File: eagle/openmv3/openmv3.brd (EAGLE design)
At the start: 35.6 x 44.5 mm, 60 parts, among them Q1 MOSFET, U1 STM32F765VGT6, U2 OV7725, U3 BD33IA, X1 47571-0001

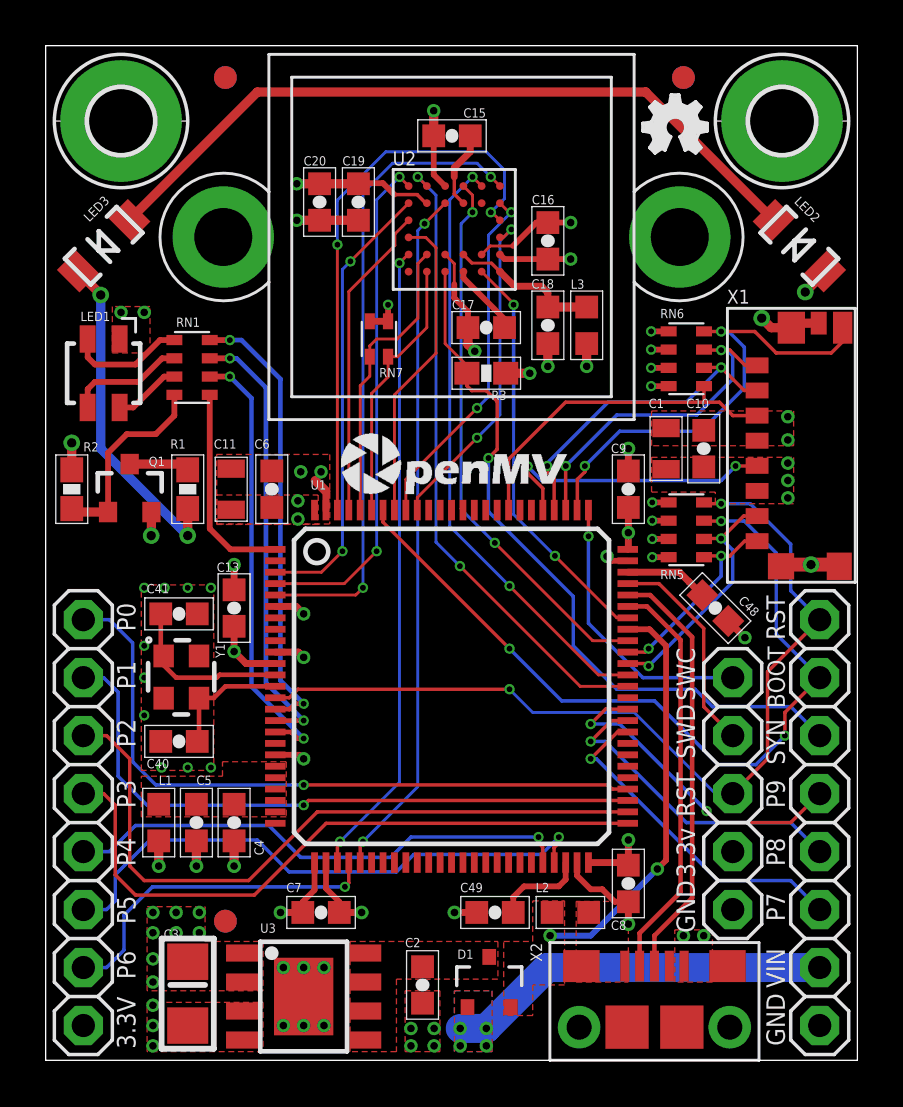
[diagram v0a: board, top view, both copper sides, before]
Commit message: Added 3 more I/O pins
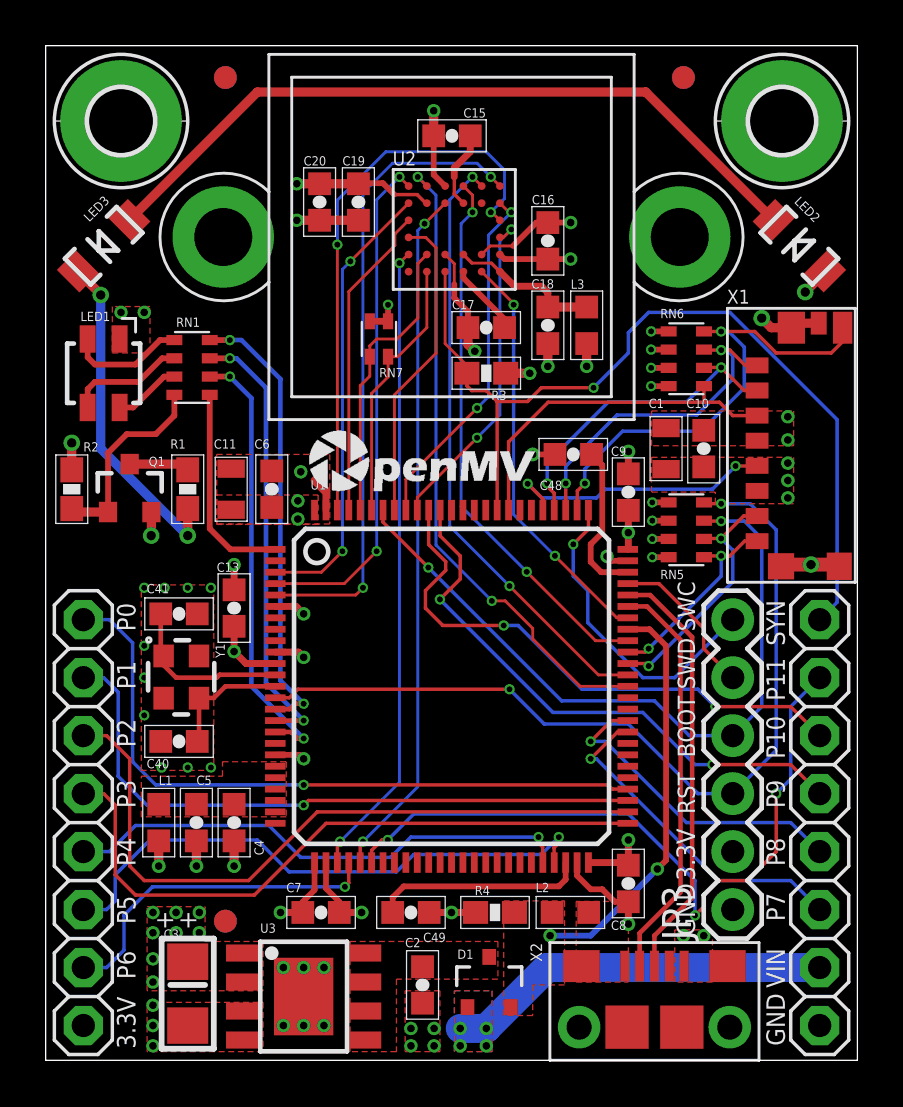
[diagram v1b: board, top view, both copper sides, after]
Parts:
- added R4: 100K, sfe:0603-RES
- JP3: device pinhead:1X05 -> SparkFun-Connectors:1X06
- moved LOGO1 38.1 mm to (20.8, 2.03), flipped to the bottom
- moved C48 9.17 mm to (23.1, 26.5), turned to 180 degrees
- moved JP3 5.08 mm to (30.1, 6.60), turned to 90 degrees
- moved C49 3.68 mm to (16.0, 6.48), turned to 0 degrees
- moved U$4 1.40 mm to (11.4, 24.8)
- moved C9 0.13 mm to (25.5, 24.9)
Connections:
- net N$1 renamed VREFH
- net N$10 renamed LED_IR_4
- net N$12 renamed VDDA
- net N$13 renamed AVDD
- net N$14 renamed LED_IR_3
- net N$15 renamed DVDD
- net N$17 renamed LED_IR_5
- net N$2 renamed OSC_OUT
- net N$3 renamed VREFN
- net N$4 renamed OSC_IN
- net N$5 renamed LED_IR_2
- net N$6 renamed LED_B_2
- net N$7 renamed VBUS_PRE
- net N$8 renamed LED_R_2
- net N$9 renamed LED_G_2
- removed net EXPST: U1.55
- removed net FREX: U1.56
- removed net TIM4_CH3: JP1.4, U1.61
- new net ADC: JP1.2, U1.31
- new net CAN_RX: JP1.4, U1.89
- new net CAN_TX: JP1.3, U1.90
- net BOOT0: now also JP3.4; no longer JP1.2
- net FSIN: now also JP1.1, U1.84; no longer JP1.3
- net GND: now also JP3.1, R4.1; no longer JP3.5
- net NRST: no longer JP1.1
- net SWCLK: now also JP3.6; no longer JP3.1
- net SWDIO: now also JP3.5; no longer JP3.2
- net VBUS: now also R4.2
- net VCC: now also JP3.2; no longer JP3.4
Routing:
- net ADC: track 0.00 -> 31.5 mm, vias 0 -> 3
- net CAN_RX: track 0.00 -> 24.8 mm, vias 0 -> 2
- net CAN_TX: track 0.00 -> 24.6 mm, vias 0 -> 2
- net TIM4_CH3: track 14.2 -> 0.00 mm, vias 2 -> 0
- net FSIN: track 31.8 -> 39.8 mm
- net VCAP1: track 4.03 -> 9.31 mm
- net BOOT0: track 36.2 -> 31.7 mm, vias 3 -> 2
- net VCAP2: track 3.69 -> 6.92 mm
- net SWDIO: track 9.37 -> 6.83 mm
- net SWCLK: track 12.3 -> 13.9 mm
- net NRST: track 39.7 -> 38.1 mm
- net GND: track 45.0 -> 46.0 mm
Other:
- board text added: "+"
- board text added: "11/28/2016"
- board text added: "Max VIN: 5V"
- board text added: "P10"
- board text added: "P10=PB4/CAN_TX"
- board text added: "P11"
- board text added: "P11=PA7/ADC2"
- board text added: "P9=PB3/CAN_RX"
- board text removed: "10/15/2016"
- board text removed: "3.3v"
- board text removed: "Max voltage: 5v"
- board text removed: "P9=PD14/SERVO3"

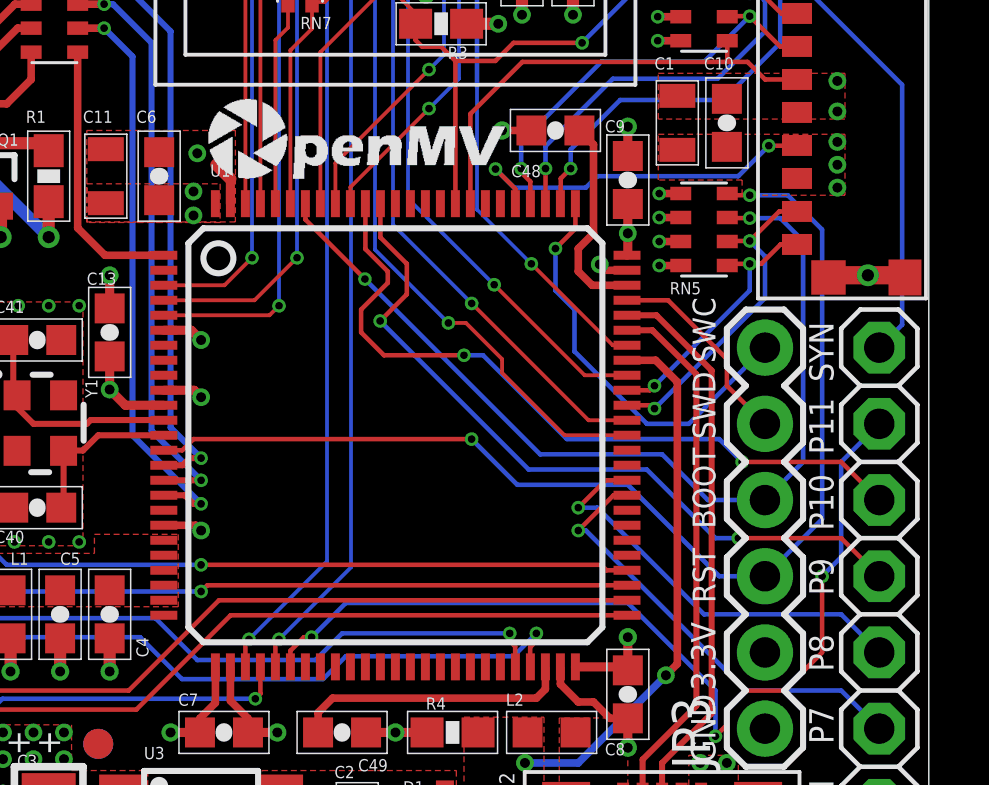
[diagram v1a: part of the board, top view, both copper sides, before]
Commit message: Swap BOOT0 and RST pins
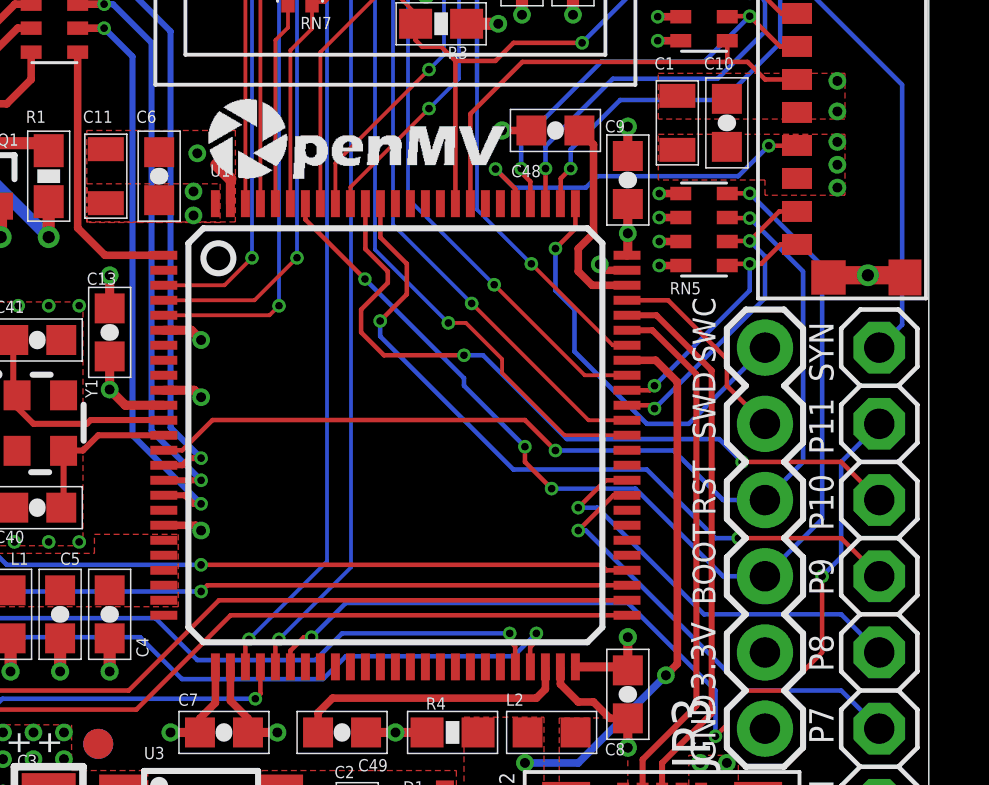
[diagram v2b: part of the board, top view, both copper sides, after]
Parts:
- R4: value 100K -> 470K
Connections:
- net BOOT0: now also JP3.3, RN5.8; no longer JP3.4, RN5.7
- net GND: now also RN5.1; no longer RN5.2
- net NRST: now also JP3.4, RN5.7; no longer JP3.3, RN5.8
- net VCC: now also RN5.2; no longer RN5.1
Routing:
- net NRST: track 38.1 -> 33.0 mm
- net BOOT0: track 31.7 -> 36.5 mm, vias 2 -> 4
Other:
- board text added: "http://www.openmv.io"
- board text removed: "https://openmv.io"

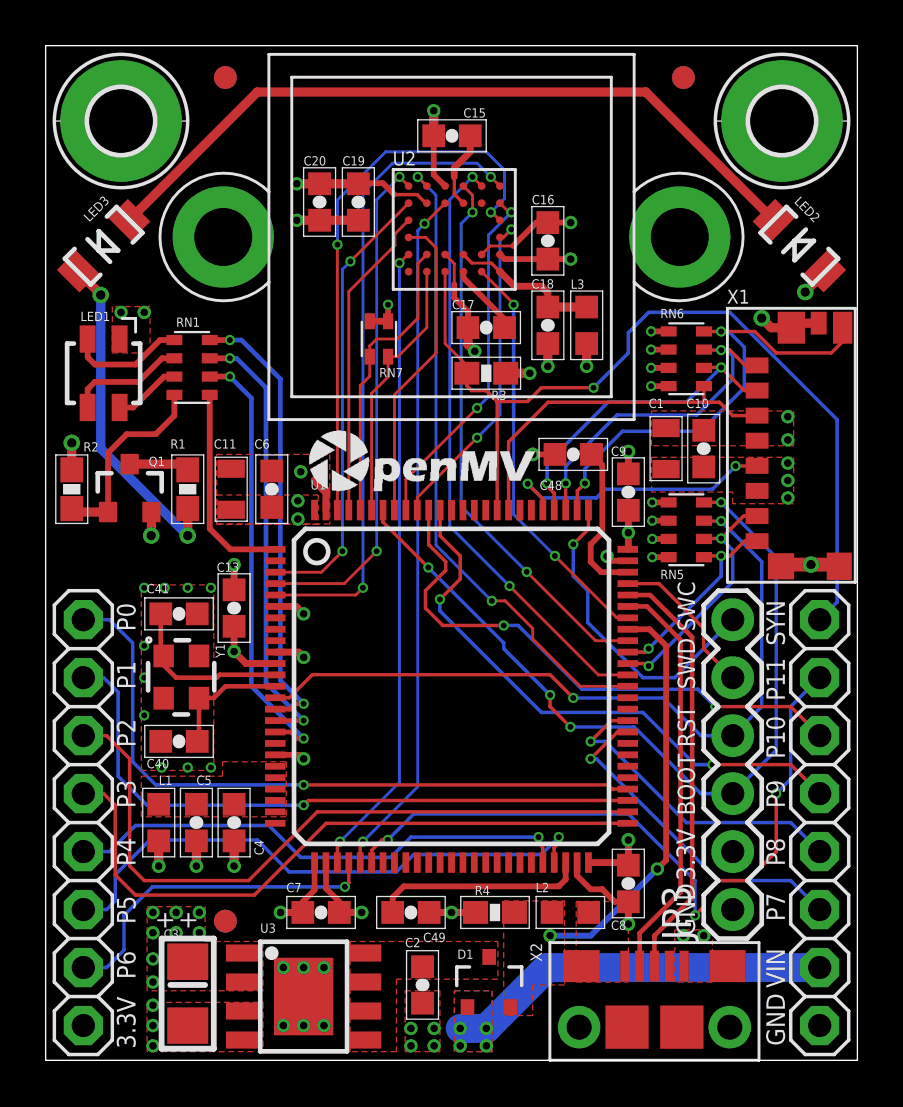
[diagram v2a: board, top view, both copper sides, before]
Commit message: Update OpenMV3 design files.
* Fix silk screen.
* Fix power diode part number.
* Replace IR LEDs.
* Revert last two commits.
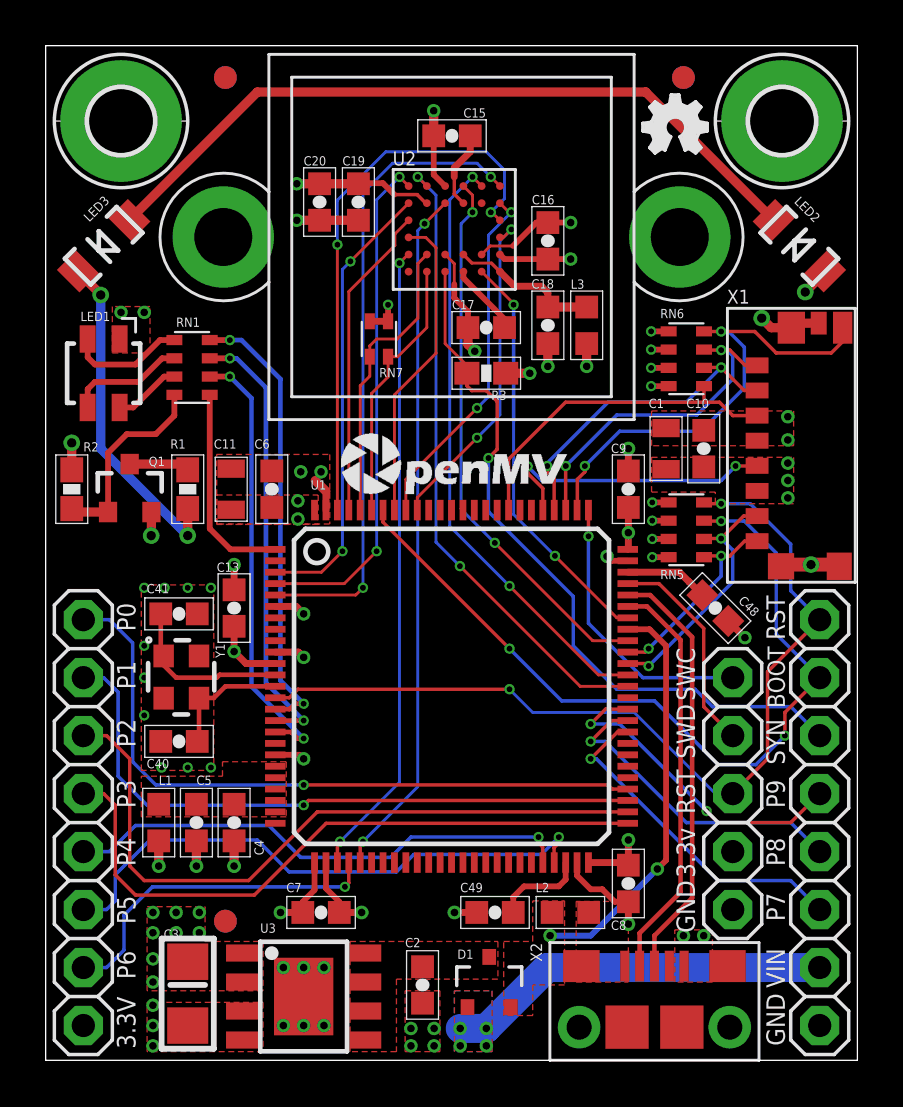
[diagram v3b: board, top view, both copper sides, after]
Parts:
- removed R4: 470K, sfe:0603-RES
- D1: value BAT54C -> PMEG2005CT
- JP3: device SparkFun-Connectors:1X06 -> pinhead:1X05
- moved LOGO1 38.1 mm to (26.2, 39.8), flipped to the top
- moved C48 9.17 mm to (29.3, 19.8), turned to 315 degrees
- moved JP3 5.08 mm to (30.1, 11.7), turned to 270 degrees
- moved C49 3.68 mm to (19.7, 6.48), turned to 180 degrees
- moved U$4 1.40 mm to (12.8, 24.6)
- moved C9 0.13 mm to (25.5, 25.0)
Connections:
- net AVDD renamed N$13
- net DVDD renamed N$15
- net LED_B_2 renamed N$6
- net LED_G_2 renamed N$9
- net LED_IR_2 renamed N$5
- net LED_IR_3 renamed N$14
- net LED_IR_4 renamed N$10
- net LED_IR_5 renamed N$17
- net LED_R_2 renamed N$8
- net OSC_IN renamed N$4
- net OSC_OUT renamed N$2
- net VBUS_PRE renamed N$7
- net VDDA renamed N$12
- net VREFH renamed N$1
- net VREFN renamed N$3
- removed net ADC: JP1.2, U1.31
- removed net CAN_RX: JP1.4, U1.89
- removed net CAN_TX: JP1.3, U1.90
- new net EXPST: U1.55
- new net FREX: U1.56
- new net TIM4_CH3: JP1.4, U1.61
- net BOOT0: now also JP1.2, RN5.7; no longer JP3.3, RN5.8
- net FSIN: now also JP1.3; no longer JP1.1, U1.84
- net GND: now also JP3.5, RN5.2; no longer JP3.1, R4.1, RN5.1
- net NRST: now also JP1.1, JP3.3, RN5.8; no longer JP3.4, RN5.7
- net SWCLK: now also JP3.1; no longer JP3.6
- net SWDIO: now also JP3.2; no longer JP3.5
- net VBUS: no longer R4.2
- net VCC: now also JP3.4, RN5.1; no longer JP3.2, RN5.2
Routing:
- net ADC: track 31.5 -> 0.00 mm, vias 3 -> 0
- net CAN_RX: track 25.1 -> 0.00 mm, vias 2 -> 0
- net CAN_TX: track 24.6 -> 0.00 mm, vias 2 -> 0
- net TIM4_CH3: track 0.00 -> 14.2 mm, vias 0 -> 2
- net FSIN: track 39.8 -> 31.8 mm
- net NRST: track 33.0 -> 39.7 mm
- net VCAP1: track 9.31 -> 4.03 mm
- net VCAP2: track 6.92 -> 3.69 mm
- net SWDIO: track 6.83 -> 9.37 mm
- net SWCLK: track 13.9 -> 12.3 mm
- net GND: track 46.0 -> 45.0 mm
- net BOOT0: track 36.5 -> 36.2 mm, vias 4 -> 3
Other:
- board text added: "10/15/2016"
- board text added: "3.3v"
- board text added: "Max voltage: 5v"
- board text added: "P9=PD14/SERVO3"
- board text added: "https://openmv.io"
- board text removed: "+"
- board text removed: "11/28/2016"
- board text removed: "Max VIN: 5V"
- board text removed: "P10"
- board text removed: "P10=PB4/CAN_TX"
- board text removed: "P11"
- board text removed: "P11=PA7/ADC2"
- board text removed: "P9=PB3/CAN_RX"
- board text removed: "http://www.openmv.io"

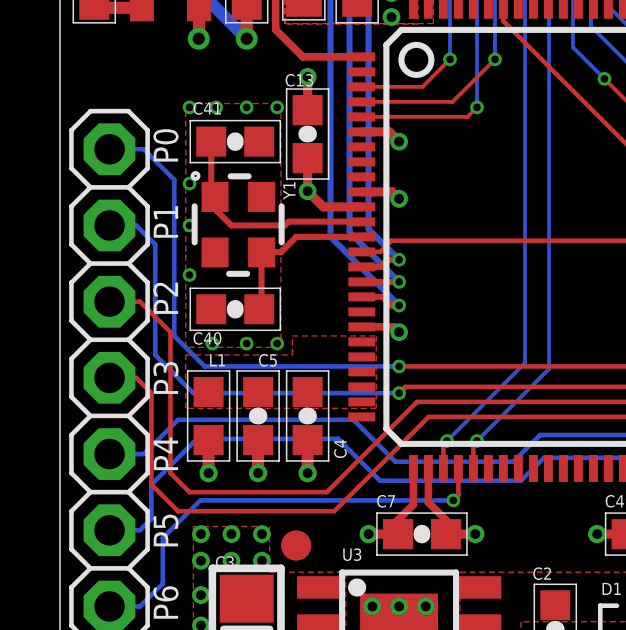
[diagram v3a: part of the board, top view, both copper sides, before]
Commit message: Add missing parts values to OMV3 design files.
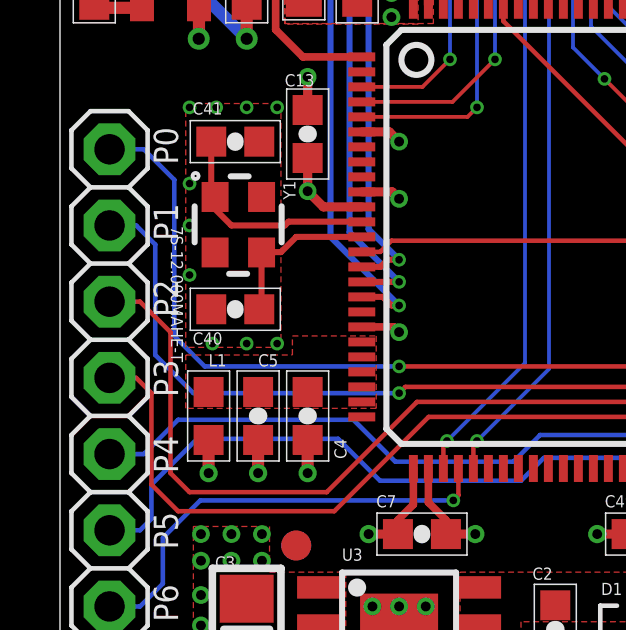
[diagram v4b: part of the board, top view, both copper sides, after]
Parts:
- removed H6: MOUNT-PAD-ROUND2.8, holes:2,8-PAD
- added H1: MOUNT-PAD-ROUND2.8, holes:2,8-PAD
- L1, L2, L3: value (none) -> MPZ1608S181ATAH0
- X2: value (none) -> MICROUSB-RIGHT
- Y1: value (none) -> 7S-12.000MAHE-T
- moved H2 29.0 mm to (32.3, 41.1), turned to 270 degrees
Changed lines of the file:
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@@
 </autorouter>
 <elements>
-<element name="H6" library="holes" package="2,8-PAD" value="MOUNT-PAD-ROUND2.8" x="32.258" y="41.148" smashed="yes" rot="R270"/>
+<element name="H2" library="holes" package="2,8-PAD" value="MOUNT-PAD-ROUND2.8" x="32.258" y="41.148" smashed="yes" rot="R270"/>
 <element name="C40" library="sfe" package="0603-CAP" value="12pF" x="5.842" y="13.97" smashed="yes">
 <attribute name="NAME" x="4.4232125" y="12.7943125" size="0.4064" layer="25" font="vector" ratio="20"/>
@@
 <attribute name="VALUE" x="20.857" y="33.2795" size="0.4064" layer="27" rot="R270"/>
 </element>
-<element name="L3" library="sfe" package="0603" value="" x="23.7" y="32.2" smashed="yes" rot="R270">
+<element name="L3" library="sfe" package="0603" value="MPZ1608S181ATAH0" x="23.7" y="32.2" smashed="yes" rot="R270">
 <attribute name="NAME" x="23" y="33.8" size="0.4064" layer="25" font="vector" ratio="20"/>
 <attribute name="VALUE" x="22.557" y="33.2795" size="0.4064" layer="27" rot="R270"/>
@@
 </element>
 <element name="LM1" library="omnivision" package="LENSMOUNT-20MM" value="LENSMOUNT20MM" x="17.78" y="36.068" smashed="yes"/>
-<element name="H2" library="holes" package="2,8-PAD" value="MOUNT-PAD-ROUND2.8" x="3.302" y="41.148" smashed="yes" rot="R90"/>
+<element name="H1" library="holes" package="2,8-PAD" value="MOUNT-PAD-ROUND2.8" x="3.302" y="41.148" smashed="yes" rot="R90"/>
 <element name="RN6" library="resistor-dil" package="EXBV8V" value="10K" x="28.067" y="30.734" smashed="yes" rot="R270">
 <attribute name="OC_NEWARK" value="unknown" x="28.067" y="30.734" size="1.778" layer="27" rot="R270" display="off"/>
@@
 <attribute name="VALUE" x="29.337" y="25.146" size="0.4064" layer="27" font="vector" ratio="20" rot="R270"/>
 </element>
-<element name="L1" library="sfe" package="0603" value="" x="4.953" y="10.414" smashed="yes" rot="R270">
+<element name="L1" library="sfe" package="0603" value="MPZ1608S181ATAH0" x="4.953" y="10.414" smashed="yes" rot="R270">
 <attribute name="NAME" x="4.953" y="12.065" size="0.4064" layer="25" font="vector" ratio="20"/>
 <attribute name="VALUE" x="3.81" y="11.4935" size="0.4064" layer="27" rot="R270"/>
@@
 <attribute name="VALUE" x="0.40201875" y="30.4100125" size="0.4064" layer="27" font="vector" ratio="20"/>
 </element>
-<element name="Y1" library="mux" package="CRYSTAL-2.5X2.0" value="" x="5.969" y="16.764" smashed="yes" rot="SR270">
+<element name="Y1" library="mux" package="CRYSTAL-2.5X2.0" value="7S-12.000MAHE-T" x="5.969" y="16.764" smashed="yes" rot="SR270">
 <attribute name="NAME" x="7.84891875" y="17.6273875" size="0.4064" layer="25" font="vector" ratio="20" rot="SR90"/>
 <attribute name="VALUE" x="3.693" y="16.74200625" size="0.4064" layer="25" rot="SR270"/>
@@
 <attribute name="VALUE" x="-1.524" y="20.574" size="1.27" layer="27" rot="R270"/>
 </element>
-<element name="L2" library="sfe" package="0603" value="" x="22.987" y="6.477" smashed="yes" rot="R180">
+<element name="L2" library="sfe" package="0603" value="MPZ1608S181ATAH0" x="22.987" y="6.477" smashed="yes" rot="R180">
 <attribute name="NAME" x="21.463" y="7.366" size="0.4064" layer="25" font="vector" ratio="20"/>
 <attribute name="VALUE" x="24.0665" y="7.62" size="0.4064" layer="27" rot="R180"/>
@@
 <attribute name="VALUE" x="12.645" y="15.288" size="1.27" layer="27"/>
 </element>
-<element name="X2" library="MF_Connectors" package="MICROUSB-RIGHT" value="" x="26.67" y="2.8575" smashed="yes">
+<element name="X2" library="MF_Connectors" package="MICROUSB-RIGHT" value="MICROUSB-RIGHT" x="26.67" y="2.8575" smashed="yes">
 <attribute name="NAME" x="21.7475" y="4.318" size="0.508" layer="25" font="vector" ratio="16" rot="R90"/>
 </element>
